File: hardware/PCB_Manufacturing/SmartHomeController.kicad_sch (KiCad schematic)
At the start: 11 parts, among them Q1 BT136-600E, Q2 BT136-600E, Q3 BT136-600E, Q4 BT136-600E, U1 ESP32-WROOM-32, U2 MOC3021, U3 MOC3021, U4 MOC3021, U5 MOC3021, U6 4N25, U7 AMS1117-5.0

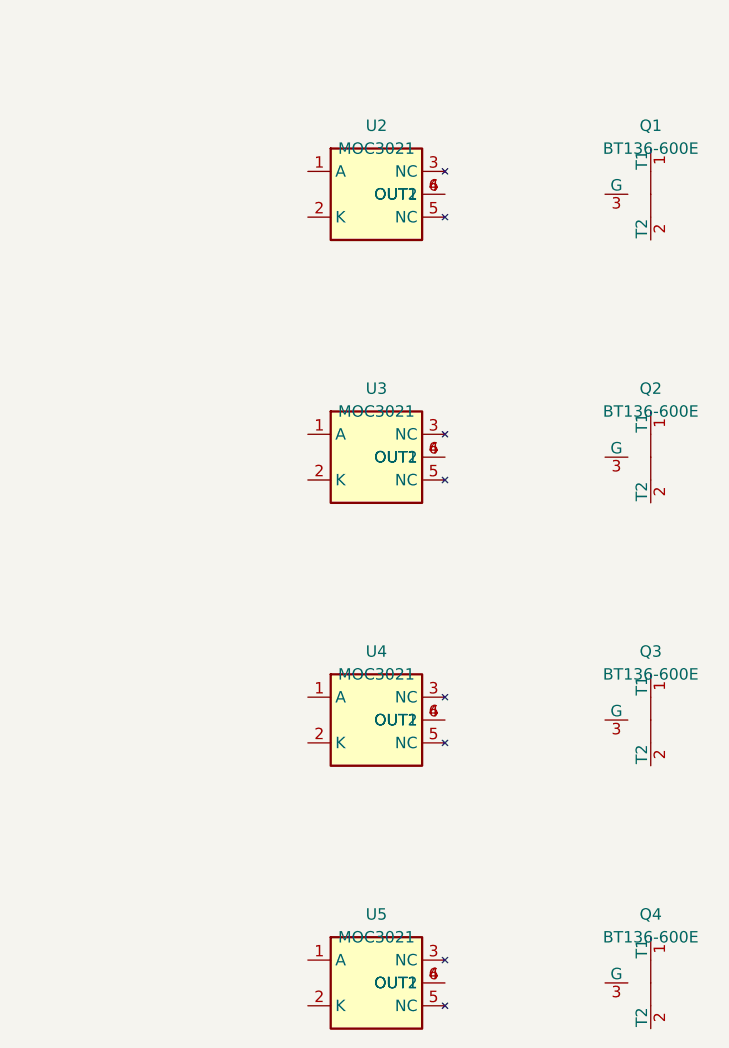
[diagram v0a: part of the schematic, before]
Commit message: Fix code review issues: MOC3021 pin overlap and TRIAC gate net assignments
Co-authored-by: Gokul3611 <177666785+Gokul3611@users.noreply.github.com>
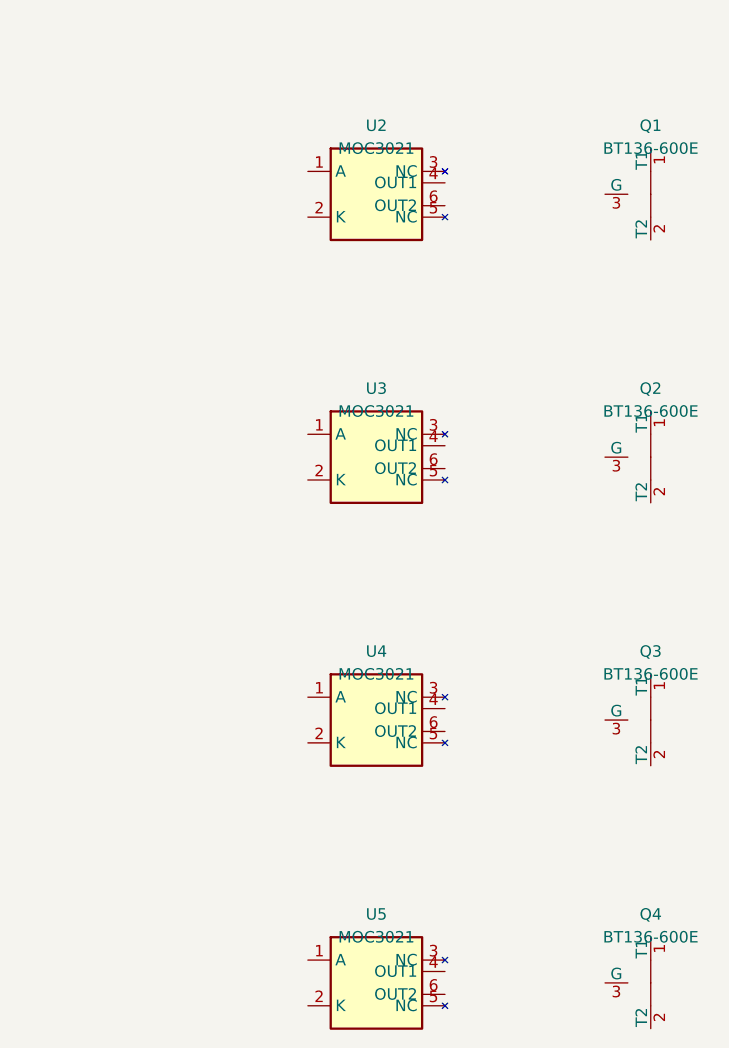
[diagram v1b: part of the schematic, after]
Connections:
- net at U2.4 (OUT1): no longer U2.6 (OUT2)
- net at U3.4 (OUT1): no longer U3.6 (OUT2)
- net at U4.4 (OUT1): no longer U4.6 (OUT2)
- net at U5.4 (OUT1): no longer U5.6 (OUT2)

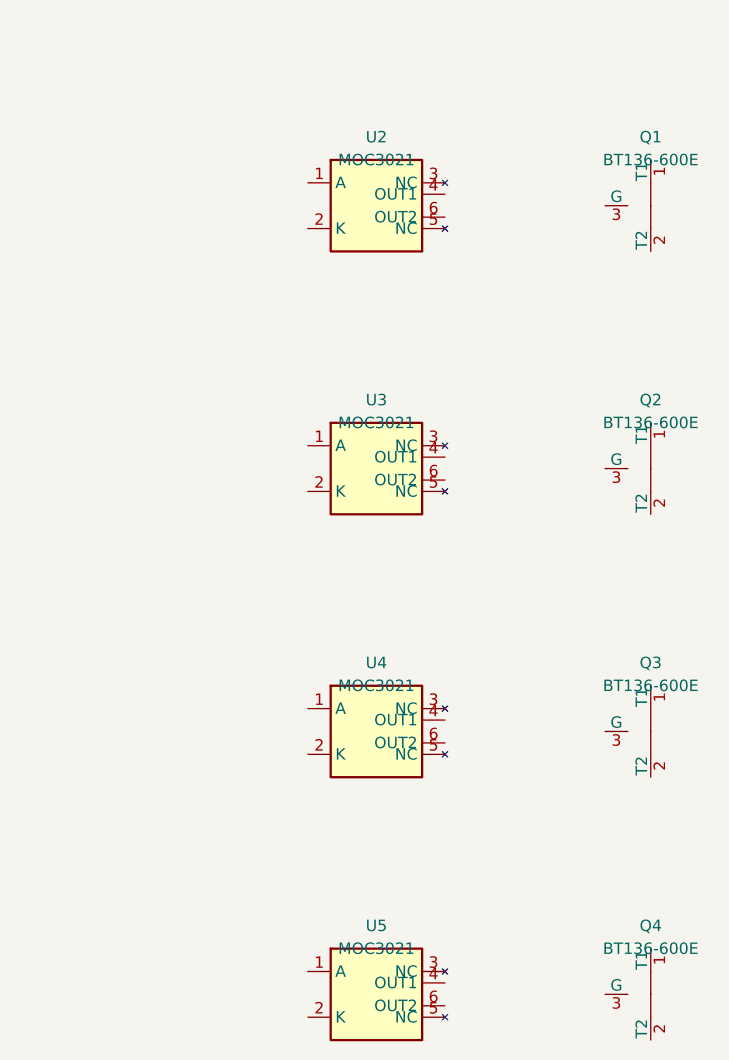
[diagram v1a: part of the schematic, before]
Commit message: Improve design: Increase MOC3021 pin spacing, enforce strict isolation keepout, add JLCPCB stackup specs
Co-authored-by: Gokul3611 <177666785+Gokul3611@users.noreply.github.com>
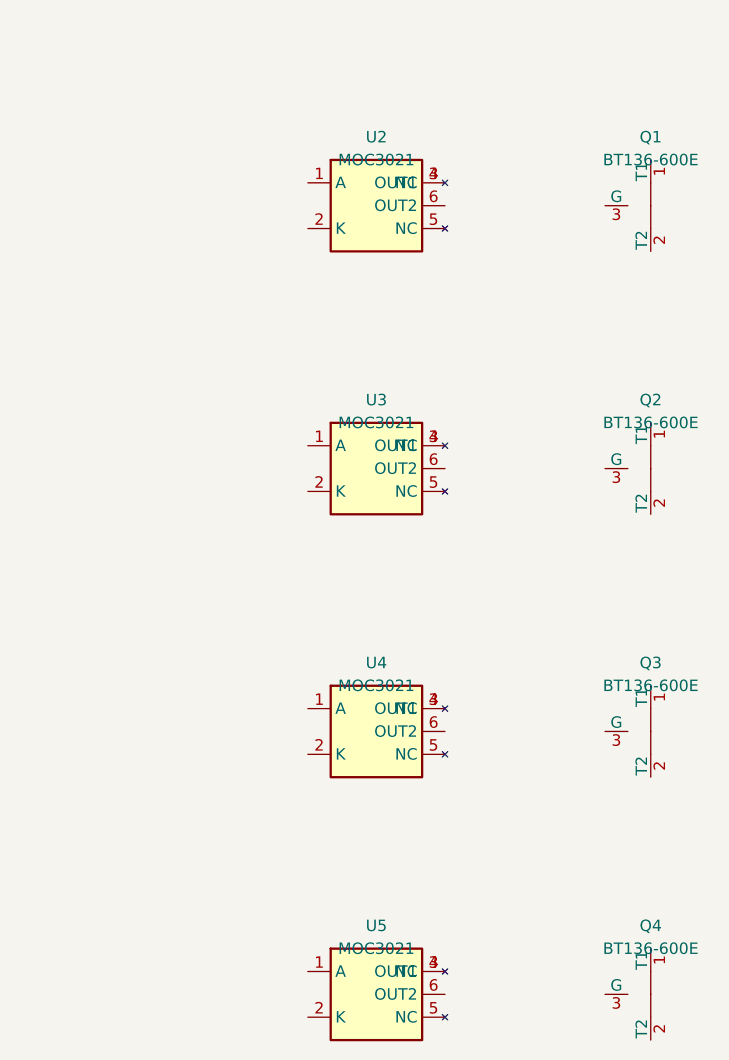
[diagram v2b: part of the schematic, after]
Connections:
- net at U2.3 (NC): now also U2.4 (OUT1)
- net at U3.3 (NC): now also U3.4 (OUT1)
- net at U4.3 (NC): now also U4.4 (OUT1)
- net at U5.3 (NC): now also U5.4 (OUT1)
